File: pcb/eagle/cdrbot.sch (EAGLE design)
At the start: 28 parts, among them IC1 PIC18F25K50, J1 CON_HEADER_1X06-PTH_M, J12 ICSP, J13 CON_HEADER_1X05-PTH_M, J2 CON_HEADER_1X06-PTH_M, J3 CON_HEADER_1X06-PTH_M, J4 CON_HEADER_1X08-PTH_M, J5 CON_HEADER_1X08-PTH_M, J6 CON_HEADER_1X08-PTH_M, J7 CON_HEADER_1X03-PTH_M, J8 CON_HEADER_1X03-PTH_M, J9 CON_HEADER_1X03-PTH_M, SW1 RESET, SW2 PRG, X1 VIN

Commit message: Nueva version del PCB
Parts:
- removed J7, J8, J9: CON_HEADER_1X03-PTH_M, gary:CON_HEADER_1X03-PTH_M
- removed JP1: USB-MICROB, SparkFun-Connectors:USB-MICROB
- removed X1: VIN, con-wago-508:W237-02P
- added BATERIA, SWITCH: CON_HEADER_1X02-PTH-M, gary:CON_HEADER_1X02-PTH-M
- added C4, C5: 22pF, gary:CAPACITOR-DECOUPLING
- added SJ1: VBUS, jumper:SJ
- added XTAL1: 20MHz, gary:OSC_XTAL-HC-49UV
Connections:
- removed net RA6: IC1.OSC2, J13.4
- removed net RA7: IC1.OSC1, R2.1, SW2.3
- removed net RC1: IC1.RC1, J9.2
- new net N$2: BATERIA.1, SWITCH.2
- new net OSC1: C5.1, IC1.OSC1, XTAL1.1
- new net OSC2: C4.1, IC1.OSC2, XTAL1.2
- new net VBUS: SJ1.2, USB1USB.VUSB
- net 5V: now also SJ1.1, SWITCH.1; no longer J8.1, J8.2, J8.3, JP1.VBUS, USB1USB.VUSB, X1-1.KL
- net D+: no longer JP1.D+
- net D-: no longer JP1.D-
- net GND: now also BATERIA.2, C4.2, C5.2; no longer J7.1, J7.2, J7.3, JP1.GND, X1-2.KL
- net RB4: now also R2.1, SW2.3
- net RC0: no longer J9.3
- net RC2: now also J13.4; no longer J9.1

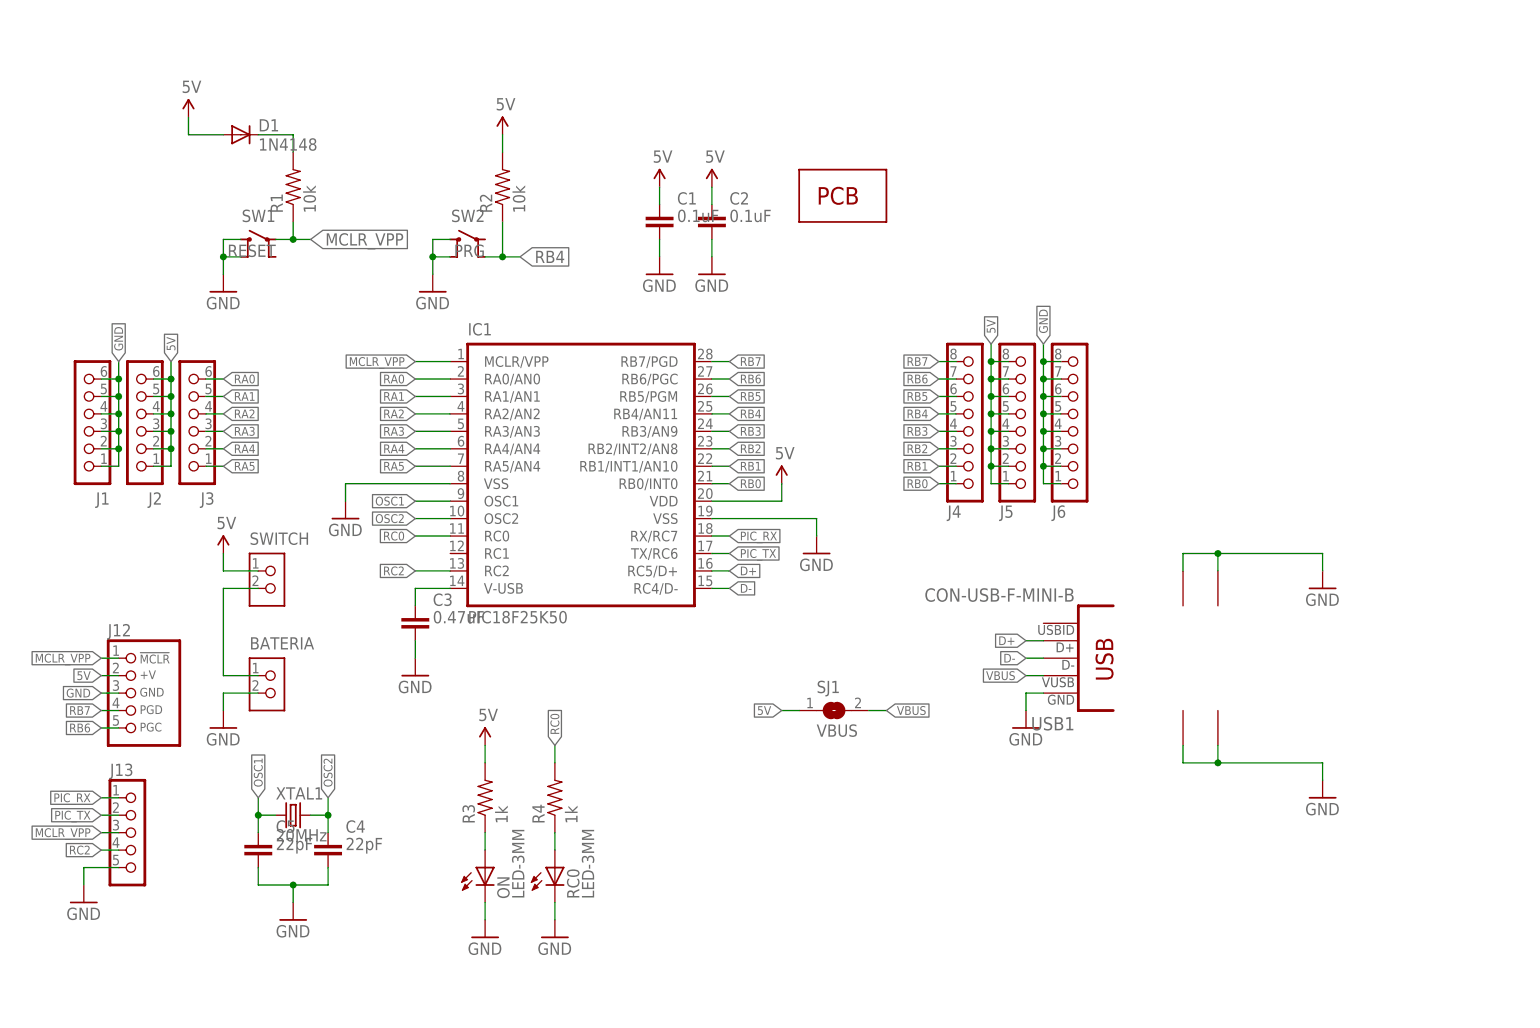
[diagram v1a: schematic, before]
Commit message: Added On/Off switch, increase cable holes, removed diode
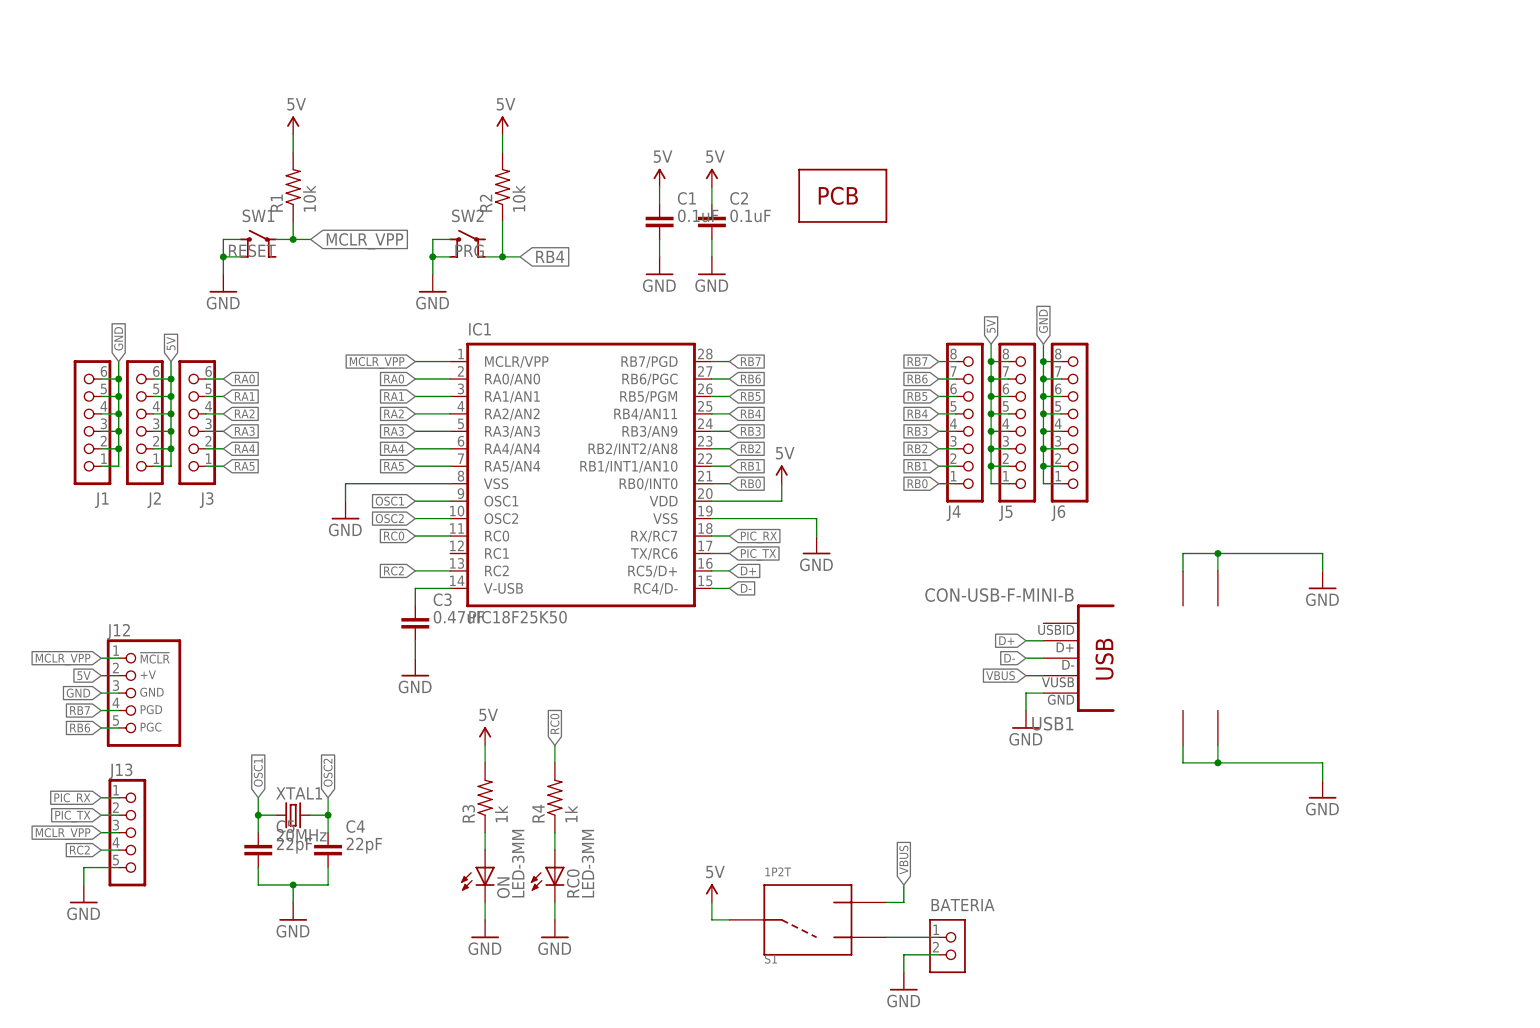
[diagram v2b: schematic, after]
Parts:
- removed D1: 1N4148, SparkFun:DIODEPTH2
- removed SJ1: VBUS, jumper:SJ
- removed SWITCH: CON_HEADER_1X02-PTH-M, gary:CON_HEADER_1X02-PTH-M
- added S1: 1P2T, gary:1P2T
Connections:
- removed net N$2: BATERIA.1, SWITCH.2
- net 5V: now also R1.2, S1.P$1; no longer D1.A, SJ1.1, SWITCH.1
- net N$1: now also BATERIA.1, S1.P$2; no longer D1.C, R1.2
- net VBUS: now also S1.P$3; no longer SJ1.2
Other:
- moved on the sheet: BATERIA
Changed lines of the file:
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@@
 <setting verticaltext="up"/>
 </settings>
-<grid distance="0.1" unitdist="inch" unit="inch" style="dots" multiple="1" display="yes" altdistance="0.01" altunitdist="inch" altunit="inch"/>
+<grid distance="0.1" unitdist="inch" unit="inch" style="lines" multiple="1" display="no" altdistance="0.01" altunitdist="inch" altunit="inch"/>
 <layers>
 <layer number="1" name="Top" color="4" fill="1" visible="no" active="no"/>
@@
 <layer number="109" name="fp9" color="7" fill="1" visible="no" active="yes"/>
 <layer number="110" name="fp0" color="7" fill="1" visible="no" active="yes"/>
+<layer number="111" name="LPC17xx" color="7" fill="1" visible="yes" active="yes"/>
+<layer number="112" name="tSilk" color="7" fill="1" visible="yes" active="yes"/>
 <layer number="116" name="Patch_BOT" color="9" fill="4" visible="yes" active="yes"/>
 <layer number="121" name="_tsilk" color="7" fill="1" visible="yes" active="yes"/>
@@
 <layer number="124" name="bTestmark" color="7" fill="1" visible="no" active="yes"/>
 <layer number="125" name="_tNames" color="7" fill="1" visible="yes" active="yes"/>
+<layer number="126" name="_bNames" color="7" fill="1" visible="yes" active="yes"/>
+<layer number="127" name="_tValues" color="7" fill="1" visible="yes" active="yes"/>
+<layer number="128" name="_bValues" color="7" fill="1" visible="yes" active="yes"/>
 <layer number="131" name="tAdjust" color="7" fill="1" visible="no" active="yes"/>
 <layer number="132" name="bAdjust" color="7" fill="1" visible="no" active="yes"/>
 <layer number="144" name="Drill_legend" color="7" fill="1" visible="yes" active="yes"/>
 <layer number="151" name="HeatSink" color="7" fill="1" visible="yes" active="yes"/>
+<layer number="152" name="_bDocu" color="7" fill="1" visible="yes" active="yes"/>
 <layer number="199" name="Contour" color="7" fill="1" visible="yes" active="yes"/>
 <layer number="200" name="200bmp" color="1" fill="10" visible="yes" active="yes"/>
@@
 <layer number="223" name="223bmp" color="24" fill="1" visible="no" active="no"/>
 <layer number="224" name="224bmp" color="25" fill="1" visible="no" active="no"/>
+<layer number="248" name="Housing" color="7" fill="1" visible="yes" active="yes"/>
+<layer number="249" name="Edge" color="7" fill="1" visible="yes" active="yes"/>
 <layer number="250" name="Descript" color="7" fill="1" visible="no" active="no"/>
 <layer number="251" name="SMDround" color="7" fill="1" visible="no" active="no"/>
@@
 <part name="U$21" library="gary" deviceset="GND" device=""/>
 <part name="U$22" library="gary" deviceset="GND" device=""/>
-<part name="D1" library="SparkFun" deviceset="DIODE" device="PTH2" value="1N4148"/>
 <part name="BATERIA" library="gary" deviceset="CON_HEADER_1X02" device="-PTH-M"/>
 <part name="XTAL1" library="gary" deviceset="OSC_XTAL" device="-HC-49UV" value="20MHz"/>
@@
 <part name="C5" library="gary" deviceset="CAPACITOR" device="-DECOUPLING" value="22pF"/>
 <part name="U$23" library="gary" deviceset="GND" device=""/>
-<part name="SWITCH" library="gary" deviceset="CON_HEADER_1X02" device="-PTH-M"/>
-<part name="SJ1" library="jumper" deviceset="SJ" device="" value="VBUS"/>
+<part name="S1" library="gary" deviceset="1P2T" device=""/>
 </parts>
 <sheets>
@@
 <instance part="U$15" gate="1" x="10.16" y="30.48"/>
 <instance part="C1" gate="C" x="10.16" y="38.1"/>
-<instance part="U$16" gate="G$1" x="-53.34" y="-10.16"/>
-<instance part="U$17" gate="1" x="-53.34" y="-35.56"/>
+<instance part="U$16" gate="G$1" x="17.78" y="-60.96"/>
+<instance part="U$17" gate="1" x="45.72" y="-73.66"/>
 <instance part="PCB1" gate="G$1" x="30.48" y="38.1"/>
 <instance part="C3" gate="C" x="-25.4" y="-20.32"/>
@@
 <instance part="U$6" gate="1" x="-73.66" y="-60.96"/>
 <instance part="R1" gate="R" x="-43.18" y="43.18" rot="R90"/>
-<instance part="U$7" gate="G$1" x="-58.42" y="53.34"/>
+<instance part="U$7" gate="G$1" x="-43.18" y="50.8"/>
 <instance part="U$8" gate="G$1" x="17.78" y="43.18"/>
 <instance part="U$9" gate="1" x="17.78" y="30.48"/>
@@
 <instance part="U$21" gate="1" x="106.68" y="-15.24"/>
 <instance part="U$22" gate="1" x="106.68" y="-45.72"/>
-<instance part="D1" gate="G$1" x="-50.8" y="50.8"/>
-<instance part="BATERIA" gate="J" x="-48.26" y="-27.94"/>
+<instance part="BATERIA" gate="J" x="50.8" y="-66.04"/>
 <instance part="XTAL1" gate="X" x="-43.18" y="-48.26"/>
 <instance part="C4" gate="C" x="-38.1" y="-53.34"/>
 <instance part="C5" gate="C" x="-48.26" y="-53.34"/>
 <instance part="U$23" gate="1" x="-43.18" y="-63.5"/>
-<instance part="SWITCH" gate="J" x="-48.26" y="-12.7"/>
-<instance part="SJ1" gate="1" x="35.56" y="-33.02"/>
+<instance part="S1" gate="G$1" x="25.4" y="-63.5" rot="MR180"/>
 </instances>
 <busses>
@@
 <segment>
 <pinref part="U$17" gate="1" pin="GND"/>
-<wire x1="-48.26" y1="-30.48" x2="-53.34" y2="-30.48" width="0.1524" layer="91"/>
-<wire x1="-53.34" y1="-30.48" x2="-53.34" y2="-33.02" width="0.1524" layer="91"/>
+<wire x1="50.8" y1="-68.58" x2="45.72" y2="-68.58" width="0.1524" layer="91"/>
+<wire x1="45.72" y1="-68.58" x2="45.72" y2="-71.12" width="0.1524" layer="91"/>
 <pinref part="BATERIA" gate="J" pin="2"/>
 </segment>
@@
 <segment>
 <pinref part="U$16" gate="G$1" pin="5V"/>
-<wire x1="-53.34" y1="-12.7" x2="-53.34" y2="-10.16" width="0.1524" layer="91"/>
-<pinref part="SWITCH" gate="J" pin="1"/>
-<wire x1="-48.26" y1="-12.7" x2="-53.34" y2="-12.7" width="0.1524" layer="91"/>
+<wire x1="17.78" y1="-63.5" x2="17.78" y2="-60.96" width="0.1524" layer="91"/>
+<pinref part="S1" gate="G$1" pin="P$1"/>
+<wire x1="20.32" y1="-63.5" x2="17.78" y2="-63.5" width="0.1524" layer="91"/>
 </segment>
 <segment>
@@
 </segment>
 <segment>
-<pinref part="D1" gate="G$1" pin="A"/>
-<wire x1="-53.34" y1="50.8" x2="-58.42" y2="50.8" width="0.1524" layer="91"/>
 <pinref part="U$7" gate="G$1" pin="5V"/>
-<wire x1="-58.42" y1="50.8" x2="-58.42" y2="53.34" width="0.1524" layer="91"/>
-</segment>
-<segment>
-<pinref part="SJ1" gate="1" pin="1"/>
-<wire x1="30.48" y1="-33.02" x2="27.94" y2="-33.02" width="0.1524" layer="91"/>
-<label x="27.94" y="-33.02" size="1.27" layer="95" rot="R180" xref="yes"/>
+<pinref part="R1" gate="R" pin="2"/>
+<wire x1="-43.18" y1="50.8" x2="-43.18" y2="48.26" width="0.1524" layer="91"/>
 </segment>
 </net>
@@
 <pinref part="RC0" gate="D" pin="A"/>
 <wire x1="-5.08" y1="-50.8" x2="-5.08" y2="-53.34" width="0.1524" layer="91"/>
-</segment>
-</net>
-<net name="N$1" class="0">
-<segment>
-<pinref part="D1" gate="G$1" pin="C"/>
-<wire x1="-48.26" y1="50.8" x2="-43.18" y2="50.8" width="0.1524" layer="91"/>
-<pinref part="R1" gate="R" pin="2"/>
-<wire x1="-43.18" y1="50.8" x2="-43.18" y2="48.26" width="0.1524" layer="91"/>
 </segment>
 </net>
@@
 </segment>
 </net>
-<net name="N$2" class="0">
-<segment>
-<pinref part="BATERIA" gate="J" pin="1"/>
-<wire x1="-48.26" y1="-27.94" x2="-53.34" y2="-27.94" width="0.1524" layer="91"/>
-<wire x1="-53.34" y1="-27.94" x2="-53.34" y2="-15.24" width="0.1524" layer="91"/>
-<pinref part="SWITCH" gate="J" pin="2"/>
-<wire x1="-53.34" y1="-15.24" x2="-48.26" y2="-15.24" width="0.1524" layer="91"/>
-</segment>
-</net>
 <net name="VBUS" class="0">
-<segment>
-<pinref part="SJ1" gate="1" pin="2"/>
-<wire x1="40.64" y1="-33.02" x2="43.18" y2="-33.02" width="0.1524" layer="91"/>
-<label x="43.18" y="-33.02" size="1.27" layer="95" xref="yes"/>
-</segment>
 <segment>
 <pinref part="USB1" gate="USB" pin="VUSB"/>
@@
 <label x="63.5" y="-27.94" size="1.27" layer="95" rot="R180" xref="yes"/>
 </segment>
-</net>
+<segment>
+<wire x1="45.72" y1="-60.96" x2="45.72" y2="-58.42" width="0.1524" layer="91"/>
+<label x="45.72" y="-58.42" size="1.27" layer="95" rot="R90" xref="yes"/>
+<pinref part="S1" gate="G$1" pin="P$3"/>
+<wire x1="43.18" y1="-60.96" x2="45.72" y2="-60.96" width="0.1524" layer="91"/>
+</segment>
+</net>
+<net name="N$1" class="0">
+<segment>
+<pinref part="BATERIA" gate="J" pin="1"/>
+<pinref part="S1" gate="G$1" pin="P$2"/>
+<wire x1="50.8" y1="-66.04" x2="43.18" y2="-66.04" width="0.1524" layer="91"/>
+</segment>
+</net>

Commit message: Added support fot TSOP38238
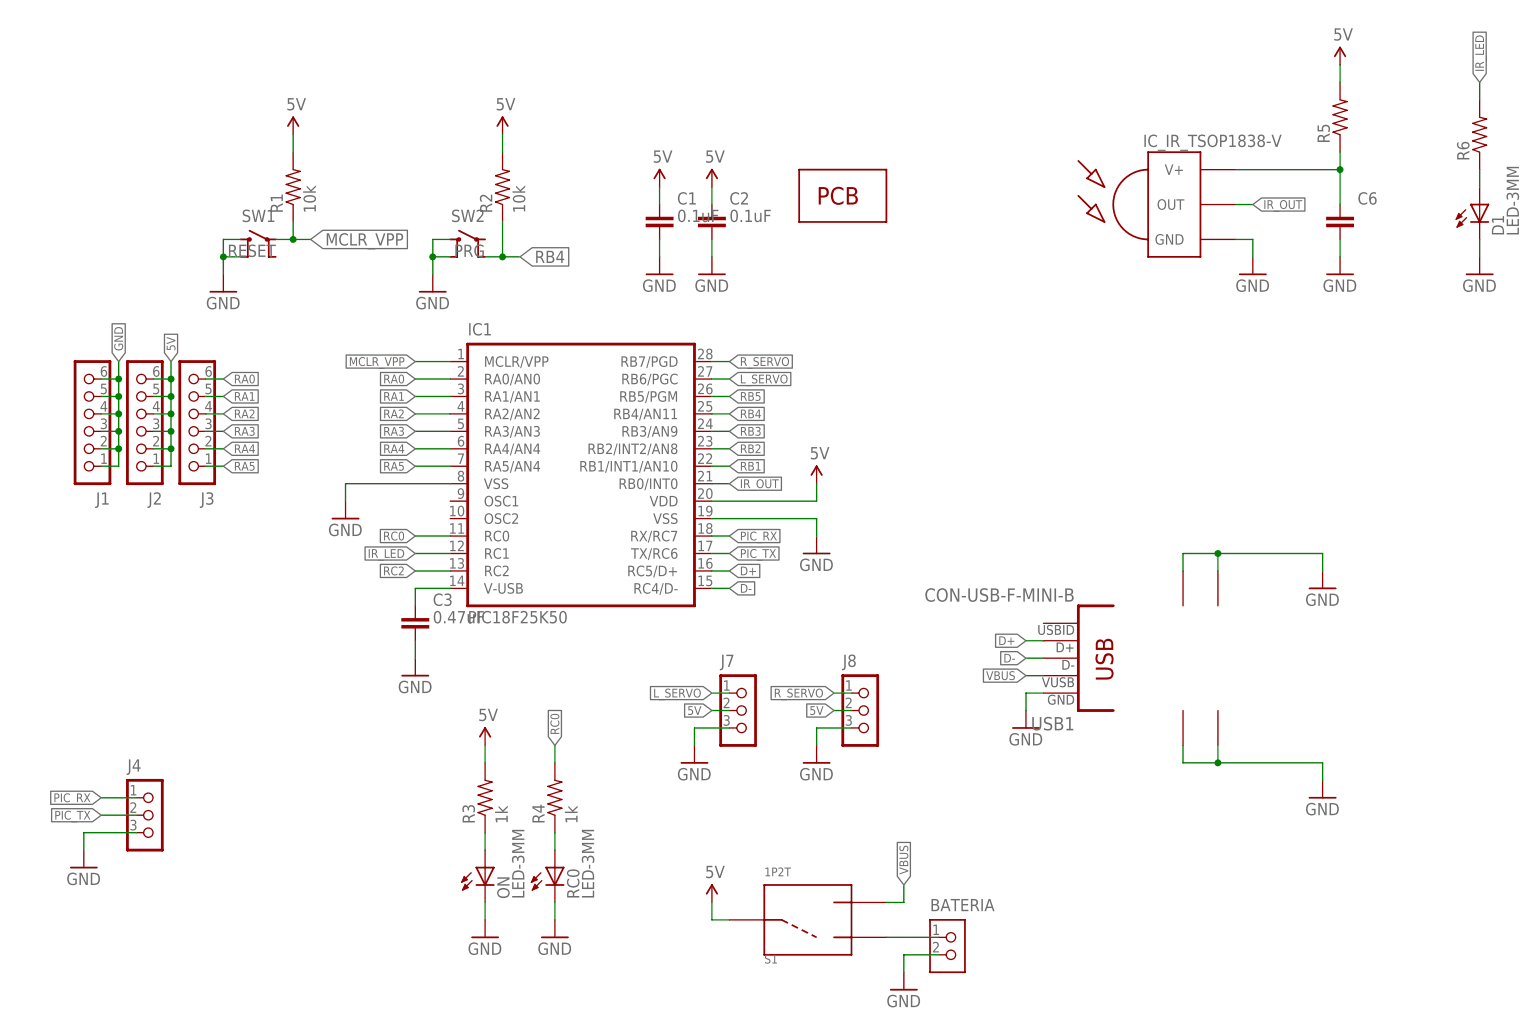
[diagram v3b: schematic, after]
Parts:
- removed C4, C5: 22pF, gary:CAPACITOR-DECOUPLING
- removed J12: ICSP, dp_devices:CON_HEADER_PRG_PIC_ICSPB
- removed J13: CON_HEADER_1X05-PTH_M, gary:CON_HEADER_1X05-PTH_M
- removed J5, J6: CON_HEADER_1X08-PTH_M, gary:CON_HEADER_1X08-PTH_M
- removed XTAL1: 20MHz, gary:OSC_XTAL-HC-49UV
- added C6: (no value), gary:CAPACITOR-DECOUPLING
- added D1: LED-3MM, gary:LED-3MM
- added IC2: IC_IR_TSOP1838-V, gary:IC_IR_TSOP1838-V
- added J7, J8: CON_HEADER_1X03-PTH_M, gary:CON_HEADER_1X03-PTH_M
- added R5, R6: (no value), gary:RESISTOR-1/4W-0.3"
- J4: value CON_HEADER_1X08-PTH_M -> CON_HEADER_1X03-PTH_M; device gary:CON_HEADER_1X08-PTH_M -> gary:CON_HEADER_1X03-PTH_M
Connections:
- removed net OSC1: C5.1, IC1.OSC1, XTAL1.1
- removed net OSC2: C4.1, IC1.OSC2, XTAL1.2
- removed net RB0: IC1.RB0/INT0, J4.1
- removed net RB6: IC1.RB6/PGC, J12.PGC, J4.7
- removed net RB7: IC1.RB7/PGD, J12.PGD, J4.8
- new net IRLED: D1.A, R6.1
- new net IR_LED: IC1.RC1, R6.2
- new net IR_OUT: IC1.RB0/INT0, IC2.OUT
- new net L_SERVO: IC1.RB6/PGC, J7.1
- new net R_SERVO: IC1.RB7/PGD, J8.1
- new net VCC_TSOP: C6.1, IC2.V+, R5.1
- net 5V: now also J7.2, J8.2, R5.2; no longer J12.+V, J5.1, J5.2, J5.3, J5.4, J5.5, J5.6, J5.7, J5.8
- net GND: now also C6.2, D1.C, IC2.GND, J4.3, J7.3, J8.3; no longer C4.2, C5.2, J12.GND, J13.5, J6.1, J6.2, J6.3, J6.4, J6.5, J6.6, J6.7, J6.8
- net MCLR_VPP: no longer J12./MCLR, J13.3
- net PIC_RX: now also J4.1; no longer J13.1
- net PIC_TX: now also J4.2; no longer J13.2
- net RB1: no longer J4.2
- net RB2: no longer J4.3
- net RB3: no longer J4.4
- net RB4: no longer J4.5
- net RB5: no longer J4.6
- net RC2: no longer J13.4
